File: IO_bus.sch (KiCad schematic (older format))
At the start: 2 parts

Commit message: Added missing signals to IO and added buffer
I've removed the /WAIT and also added a somewhat dodgy diode AND to
handle the bi-directional Dx buffer. Might work, might not.

Also cleaned up the buses and just tidied things up.
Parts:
- removed P?: CONN_01X16, symbol CONN_01X16
- added C?: 100n, symbol C
- added P?: CONN_01X14, symbol CONN_01X14
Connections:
- net labels added: VCC, ~CLK
- net labels removed: CLK, VCC_5V, ~WAIT
- wire segments 25 -> 28
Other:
- moved on the sheet: P?
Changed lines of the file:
@@
 $Descr A4 11693 8268
 encoding utf-8
-Sheet 9 16
+Sheet 11 16
 Title ""
 Date ""
@@
 Text HLabel 1850 2000 0    60   Input ~ 0
 ~WR
-Text HLabel 1850 2300 0    60   Input ~ 0
-CLK
+Text HLabel 1850 2200 0    60   Input ~ 0
+~CLK
 Text HLabel 1850 2100 0    60   BiDi ~ 0
 ~INT
-Text HLabel 1850 2200 0    60   BiDi ~ 0
-~WAIT
+Text HLabel 1800 3200 0    60   BiDi ~ 0
+D4
+Text HLabel 1800 3300 0    60   BiDi ~ 0
+D5
 Text HLabel 1800 3400 0    60   BiDi ~ 0
-D4
+D6
 Text HLabel 1800 3500 0    60   BiDi ~ 0
-D5
-Text HLabel 1800 3600 0    60   BiDi ~ 0
-D6
-Text HLabel 1800 3700 0    60   BiDi ~ 0
 D7
+Text HLabel 1800 2800 0    60   BiDi ~ 0
+D0
+Text HLabel 1800 2900 0    60   BiDi ~ 0
+D1
 Text HLabel 1800 3000 0    60   BiDi ~ 0
-D0
+D2
 Text HLabel 1800 3100 0    60   BiDi ~ 0
-D1
-Text HLabel 1800 3200 0    60   BiDi ~ 0
-D2
-Text HLabel 1800 3300 0    60   BiDi ~ 0
 D3
-Text HLabel 1850 2600 0    60   UnSpc ~ 0
-VCC_5V
-Text HLabel 1850 2700 0    60   UnSpc ~ 0
-GND
 Wire Wire Line
 	1850 1200 2100 1200
@@
 	1850 2100 2100 2100
 Wire Wire Line
-	2100 2200 1850 2200
-Wire Wire Line
-	1850 2300 2100 2300
-Wire Wire Line
-	1850 2700 2100 2700
-Wire Wire Line
-	1850 2600 2100 2600
-$Comp
-L CONN_01X16 P?
-U 1 1 57809941
-P 2300 1950
-F 0 "P?" H 2300 2800 50  0000 C CNN
-F 1 "CONN_01X16" V 2400 1950 50  0000 C CNN
-F 2 "" H 2300 1950 50  0000 C CNN
-F 3 "" H 2300 1950 50  0000 C CNN
-	1    2300 1950
-	1    0    0    -1
-$EndComp
+	1850 2200 2100 2200
+Wire Wire Line
+	1250 2500 2100 2500
 $Comp
 L CONN_01X08 P?
 U 1 1 57809978
-P 2300 3350
-F 0 "P?" H 2300 3800 50  0000 C CNN
-F 1 "CONN_01X08" V 2400 3350 50  0000 C CNN
-F 2 "" H 2300 3350 50  0000 C CNN
-F 3 "" H 2300 3350 50  0000 C CNN
-	1    2300 3350
-	1    0    0    -1
-$EndComp
+P 2300 3150
+AR Path="/578460AE/578087DE/57809978" Ref="P?"  Part="1"
+AR Path="/578460AE/57822535/57809978" Ref="P?"  Part="1"
+AR Path="/578460AE/57824229/57809978" Ref="P?"  Part="1"
+AR Path="/578460AE/57824279/57809978" Ref="P?"  Part="1"
+AR Path="/578460AE/578298A9/57809978" Ref="P?"  Part="1"
+AR Path="/578460AE/578298F9/57809978" Ref="P?"  Part="1"
+AR Path="/578460AE/57830D91/57809978" Ref="P?"  Part="1"
+AR Path="/578460AE/57831F66/57809978" Ref="P?"  Part="1"
+F 0 "P?" H 2300 3600 50  0000 C CNN
+F 1 "CONN_01X08" V 2400 3150 50  0000 C CNN
+F 2 "" H 2300 3150 50  0000 C CNN
+F 3 "" H 2300 3150 50  0000 C CNN
+	1    2300 3150
+	1    0    0    -1
+$EndComp
+Wire Wire Line
+	1800 2800 2100 2800
+Wire Wire Line
+	2100 2900 1800 2900
 Wire Wire Line
 	1800 3000 2100 3000
@@
 Wire Wire Line
 	2100 3500 1800 3500
-Wire Wire Line
-	1800 3600 2100 3600
-Wire Wire Line
-	2100 3700 1800 3700
-Text HLabel 1850 2500 0    60   Input ~ 0
+Text HLabel 1850 2300 0    60   Input ~ 0
 ~RESET
 Wire Wire Line
-	1850 2500 2100 2500
-Wire Wire Line
-	2050 2700 2050 2400
-Wire Wire Line
-	2050 2400 2100 2400
-Connection ~ 2050 2700
+	1850 2300 2100 2300
+Wire Wire Line
+	1000 2100 1000 2300
+Wire Wire Line
+	1000 2600 1000 2800
+$Comp
+L VCC #PWR?
+U 1 1 5783B273
+P 1000 2100
+AR Path="/578460AE/578087DE/5783B273" Ref="#PWR?"  Part="1"
+AR Path="/578460AE/57822535/5783B273" Ref="#PWR?"  Part="1"
+AR Path="/578460AE/57824229/5783B273" Ref="#PWR?"  Part="1"
+AR Path="/578460AE/57824279/5783B273" Ref="#PWR?"  Part="1"
+AR Path="/578460AE/578298A9/5783B273" Ref="#PWR?"  Part="1"
+AR Path="/578460AE/578298F9/5783B273" Ref="#PWR?"  Part="1"
+AR Path="/578460AE/57830D91/5783B273" Ref="#PWR?"  Part="1"
+AR Path="/578460AE/57831F66/5783B273" Ref="#PWR?"  Part="1"
+F 0 "#PWR?" H 1000 1950 50  0001 C CNN
+F 1 "VCC" H 1000 2250 50  0000 C CNN
+F 2 "" H 1000 2100 50  0000 C CNN
+F 3 "" H 1000 2100 50  0000 C CNN
+	1    1000 2100
+	1    0    0    -1
+$EndComp
+$Comp
+L GND #PWR?
+U 1 1 5783B28B
+P 1000 2800
+AR Path="/578460AE/578087DE/5783B28B" Ref="#PWR?"  Part="1"
+AR Path="/578460AE/57822535/5783B28B" Ref="#PWR?"  Part="1"
+AR Path="/578460AE/57824229/5783B28B" Ref="#PWR?"  Part="1"
+AR Path="/578460AE/57824279/5783B28B" Ref="#PWR?"  Part="1"
+AR Path="/578460AE/578298A9/5783B28B" Ref="#PWR?"  Part="1"
+AR Path="/578460AE/578298F9/5783B28B" Ref="#PWR?"  Part="1"
+AR Path="/578460AE/57830D91/5783B28B" Ref="#PWR?"  Part="1"
+AR Path="/578460AE/57831F66/5783B28B" Ref="#PWR?"  Part="1"
+F 0 "#PWR?" H 1000 2550 50  0001 C CNN
+F 1 "GND" H 1000 2650 50  0000 C CNN
+F 2 "" H 1000 2800 50  0000 C CNN
+F 3 "" H 1000 2800 50  0000 C CNN
+	1    1000 2800
+	1    0    0    -1
+$EndComp
+$Comp
+L C C?
+U 1 1 5783B2B3
+P 1000 2450
+AR Path="/578460AE/578087DE/5783B2B3" Ref="C?"  Part="1"
+AR Path="/578460AE/57822535/5783B2B3" Ref="C?"  Part="1"
+AR Path="/578460AE/57824229/5783B2B3" Ref="C?"  Part="1"
+AR Path="/578460AE/57824279/5783B2B3" Ref="C?"  Part="1"
+AR Path="/578460AE/578298A9/5783B2B3" Ref="C?"  Part="1"
+AR Path="/578460AE/578298F9/5783B2B3" Ref="C?"  Part="1"
+AR Path="/578460AE/57830D91/5783B2B3" Ref="C?"  Part="1"
+AR Path="/578460AE/57831F66/5783B2B3" Ref="C?"  Part="1"
+F 0 "C?" H 1025 2550 50  0000 L CNN
+F 1 "100n" H 1025 2350 50  0000 L CNN
+F 2 "" H 1038 2300 50  0000 C CNN
+F 3 "" H 1000 2450 50  0000 C CNN
+	1    1000 2450
+	1    0    0    -1
+$EndComp
+Wire Wire Line
+	2100 2400 1250 2400
+Wire Wire Line
+	1250 2400 1250 2200
+Wire Wire Line
+	1250 2200 1000 2200
+Connection ~ 1000 2200
+Wire Wire Line
+	1250 2500 1250 2700
+Wire Wire Line
+	1250 2700 1000 2700
+Connection ~ 1000 2700
+$Comp
+L CONN_01X14 P?
+U 1 1 5785DCD8
+P 2300 1850
+AR Path="/578460AE/578087DE/5785DCD8" Ref="P?"  Part="1"
+AR Path="/578460AE/57822535/5785DCD8" Ref="P?"  Part="1"
+AR Path="/578460AE/57824229/5785DCD8" Ref="P?"  Part="1"
+AR Path="/578460AE/57824279/5785DCD8" Ref="P?"  Part="1"
+AR Path="/578460AE/578298A9/5785DCD8" Ref="P?"  Part="1"
+AR Path="/578460AE/578298F9/5785DCD8" Ref="P?"  Part="1"
+AR Path="/578460AE/57830D91/5785DCD8" Ref="P?"  Part="1"
+AR Path="/578460AE/57831F66/5785DCD8" Ref="P?"  Part="1"
+F 0 "P?" H 2300 2600 50  0000 C CNN
+F 1 "CONN_01X14" V 2400 1850 50  0000 C CNN
+F 2 "" H 2300 1850 50  0000 C CNN
+F 3 "" H 2300 1850 50  0000 C CNN
+	1    2300 1850
+	1    0    0    -1
+$EndComp
 $EndSCHEMATC

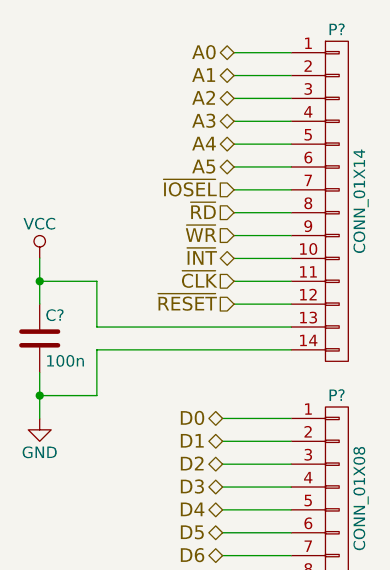
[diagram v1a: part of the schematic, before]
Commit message: Added /intack signal and a pri-encoder for /iosel
Brain fart on the diode crap. Was tired. Added a priority encoder to
enable the Dx buffer so it properly tristates when no IObus ports are
selected.

Added a NOR gate to provide a /intack signal for any board to properly
detect their interupt has been accepted but the z80. Boards will need to
figure out who the interupt is for.

Will have to add interupt priority pins to the boards to allow the
boards to put jump vectors onto the data bus to service the interrupt
This should be fairly easy, just means the service pritority of the
slots will be A-H, with A being the highest priority and H being the
lowest.

Going to replace the hex inverters with the spare NOR gates too.
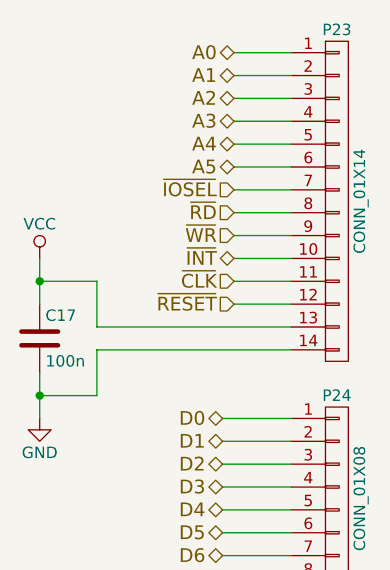
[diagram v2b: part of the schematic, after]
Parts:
- C10: renamed from C?; footprint (none) -> Capacitors_SMD:C_0805_HandSoldering
- P10: renamed from P?; footprint (none) -> Pin_Headers:Pin_Header_Straight_1x08
- P9: renamed from P?; footprint (none) -> Pin_Headers:Pin_Header_Straight_1x14
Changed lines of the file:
@@
 $Descr A4 11693 8268
 encoding utf-8
-Sheet 11 16
+Sheet 4 14
 Title ""
 Date ""
@@
 	1250 2500 2100 2500
 $Comp
-L CONN_01X08 P?
+L CONN_01X08 P10
 U 1 1 57809978
 P 2300 3150
-AR Path="/578460AE/578087DE/57809978" Ref="P?"  Part="1"
-AR Path="/578460AE/57822535/57809978" Ref="P?"  Part="1"
-AR Path="/578460AE/57824229/57809978" Ref="P?"  Part="1"
-AR Path="/578460AE/57824279/57809978" Ref="P?"  Part="1"
-AR Path="/578460AE/578298A9/57809978" Ref="P?"  Part="1"
-AR Path="/578460AE/578298F9/57809978" Ref="P?"  Part="1"
-AR Path="/578460AE/57830D91/57809978" Ref="P?"  Part="1"
-AR Path="/578460AE/57831F66/57809978" Ref="P?"  Part="1"
-F 0 "P?" H 2300 3600 50  0000 C CNN
+AR Path="/578460AE/578087DE/57809978" Ref="P10"  Part="1"
+AR Path="/578460AE/57822535/57809978" Ref="P12"  Part="1"
+AR Path="/578460AE/57824229/57809978" Ref="P14"  Part="1"
+AR Path="/578460AE/57824279/57809978" Ref="P16"  Part="1"
+AR Path="/578460AE/578298A9/57809978" Ref="P18"  Part="1"
+AR Path="/578460AE/578298F9/57809978" Ref="P20"  Part="1"
+AR Path="/578460AE/57830D91/57809978" Ref="P22"  Part="1"
+AR Path="/578460AE/57831F66/57809978" Ref="P24"  Part="1"
+F 0 "P24" H 2300 3600 50  0000 C CNN
 F 1 "CONN_01X08" V 2400 3150 50  0000 C CNN
-F 2 "" H 2300 3150 50  0000 C CNN
+F 2 "Pin_Headers:Pin_Header_Straight_1x08" H 2300 3150 50  0001 C CNN
 F 3 "" H 2300 3150 50  0000 C CNN
 	1    2300 3150
@@
 	1000 2600 1000 2800
 $Comp
-L VCC #PWR?
+L VCC #PWR027
 U 1 1 5783B273
 P 1000 2100
-AR Path="/578460AE/578087DE/5783B273" Ref="#PWR?"  Part="1"
-AR Path="/578460AE/57822535/5783B273" Ref="#PWR?"  Part="1"
-AR Path="/578460AE/57824229/5783B273" Ref="#PWR?"  Part="1"
-AR Path="/578460AE/57824279/5783B273" Ref="#PWR?"  Part="1"
-AR Path="/578460AE/578298A9/5783B273" Ref="#PWR?"  Part="1"
-AR Path="/578460AE/578298F9/5783B273" Ref="#PWR?"  Part="1"
-AR Path="/578460AE/57830D91/5783B273" Ref="#PWR?"  Part="1"
-AR Path="/578460AE/57831F66/5783B273" Ref="#PWR?"  Part="1"
-F 0 "#PWR?" H 1000 1950 50  0001 C CNN
+AR Path="/578460AE/578087DE/5783B273" Ref="#PWR027"  Part="1"
+AR Path="/578460AE/57822535/5783B273" Ref="#PWR029"  Part="1"
+AR Path="/578460AE/57824229/5783B273" Ref="#PWR031"  Part="1"
+AR Path="/578460AE/57824279/5783B273" Ref="#PWR033"  Part="1"
+AR Path="/578460AE/578298A9/5783B273" Ref="#PWR035"  Part="1"
+AR Path="/578460AE/578298F9/5783B273" Ref="#PWR037"  Part="1"
+AR Path="/578460AE/57830D91/5783B273" Ref="#PWR039"  Part="1"
+AR Path="/578460AE/57831F66/5783B273" Ref="#PWR041"  Part="1"
+F 0 "#PWR041" H 1000 1950 50  0001 C CNN
 F 1 "VCC" H 1000 2250 50  0000 C CNN
 F 2 "" H 1000 2100 50  0000 C CNN
@@
 $EndComp
 $Comp
-L GND #PWR?
+L GND #PWR028
 U 1 1 5783B28B
 P 1000 2800
-AR Path="/578460AE/578087DE/5783B28B" Ref="#PWR?"  Part="1"
-AR Path="/578460AE/57822535/5783B28B" Ref="#PWR?"  Part="1"
-AR Path="/578460AE/57824229/5783B28B" Ref="#PWR?"  Part="1"
-AR Path="/578460AE/57824279/5783B28B" Ref="#PWR?"  Part="1"
-AR Path="/578460AE/578298A9/5783B28B" Ref="#PWR?"  Part="1"
-AR Path="/578460AE/578298F9/5783B28B" Ref="#PWR?"  Part="1"
-AR Path="/578460AE/57830D91/5783B28B" Ref="#PWR?"  Part="1"
-AR Path="/578460AE/57831F66/5783B28B" Ref="#PWR?"  Part="1"
-F 0 "#PWR?" H 1000 2550 50  0001 C CNN
+AR Path="/578460AE/578087DE/5783B28B" Ref="#PWR028"  Part="1"
+AR Path="/578460AE/57822535/5783B28B" Ref="#PWR030"  Part="1"
+AR Path="/578460AE/57824229/5783B28B" Ref="#PWR032"  Part="1"
+AR Path="/578460AE/57824279/5783B28B" Ref="#PWR034"  Part="1"
+AR Path="/578460AE/578298A9/5783B28B" Ref="#PWR036"  Part="1"
+AR Path="/578460AE/578298F9/5783B28B" Ref="#PWR038"  Part="1"
+AR Path="/578460AE/57830D91/5783B28B" Ref="#PWR040"  Part="1"
+AR Path="/578460AE/57831F66/5783B28B" Ref="#PWR042"  Part="1"
+F 0 "#PWR042" H 1000 2550 50  0001 C CNN
 F 1 "GND" H 1000 2650 50  0000 C CNN
 F 2 "" H 1000 2800 50  0000 C CNN
@@
 $EndComp
 $Comp
-L C C?
+L C C10
 U 1 1 5783B2B3
 P 1000 2450
-AR Path="/578460AE/578087DE/5783B2B3" Ref="C?"  Part="1"
-AR Path="/578460AE/57822535/5783B2B3" Ref="C?"  Part="1"
-AR Path="/578460AE/57824229/5783B2B3" Ref="C?"  Part="1"
-AR Path="/578460AE/57824279/5783B2B3" Ref="C?"  Part="1"
-AR Path="/578460AE/578298A9/5783B2B3" Ref="C?"  Part="1"
-AR Path="/578460AE/578298F9/5783B2B3" Ref="C?"  Part="1"
-AR Path="/578460AE/57830D91/5783B2B3" Ref="C?"  Part="1"
-AR Path="/578460AE/57831F66/5783B2B3" Ref="C?"  Part="1"
-F 0 "C?" H 1025 2550 50  0000 L CNN
+AR Path="/578460AE/578087DE/5783B2B3" Ref="C10"  Part="1"
+AR Path="/578460AE/57822535/5783B2B3" Ref="C11"  Part="1"
+AR Path="/578460AE/57824229/5783B2B3" Ref="C12"  Part="1"
+AR Path="/578460AE/57824279/5783B2B3" Ref="C13"  Part="1"
+AR Path="/578460AE/578298A9/5783B2B3" Ref="C14"  Part="1"
+AR Path="/578460AE/578298F9/5783B2B3" Ref="C15"  Part="1"
+AR Path="/578460AE/57830D91/5783B2B3" Ref="C16"  Part="1"
+AR Path="/578460AE/57831F66/5783B2B3" Ref="C17"  Part="1"
+F 0 "C17" H 1025 2550 50  0000 L CNN
 F 1 "100n" H 1025 2350 50  0000 L CNN
-F 2 "" H 1038 2300 50  0000 C CNN
+F 2 "Capacitors_SMD:C_0805_HandSoldering" H 1038 2300 50  0001 C CNN
 F 3 "" H 1000 2450 50  0000 C CNN
 	1    1000 2450
@@
 Connection ~ 1000 2700
 $Comp
-L CONN_01X14 P?
+L CONN_01X14 P9
 U 1 1 5785DCD8
 P 2300 1850
-AR Path="/578460AE/578087DE/5785DCD8" Ref="P?"  Part="1"
-AR Path="/578460AE/57822535/5785DCD8" Ref="P?"  Part="1"
-AR Path="/578460AE/57824229/5785DCD8" Ref="P?"  Part="1"
-AR Path="/578460AE/57824279/5785DCD8" Ref="P?"  Part="1"
-AR Path="/578460AE/578298A9/5785DCD8" Ref="P?"  Part="1"
-AR Path="/578460AE/578298F9/5785DCD8" Ref="P?"  Part="1"
-AR Path="/578460AE/57830D91/5785DCD8" Ref="P?"  Part="1"
-AR Path="/578460AE/57831F66/5785DCD8" Ref="P?"  Part="1"
-F 0 "P?" H 2300 2600 50  0000 C CNN
+AR Path="/578460AE/578087DE/5785DCD8" Ref="P9"  Part="1"
+AR Path="/578460AE/57822535/5785DCD8" Ref="P11"  Part="1"
+AR Path="/578460AE/57824229/5785DCD8" Ref="P13"  Part="1"
+AR Path="/578460AE/57824279/5785DCD8" Ref="P15"  Part="1"
+AR Path="/578460AE/578298A9/5785DCD8" Ref="P17"  Part="1"
+AR Path="/578460AE/578298F9/5785DCD8" Ref="P19"  Part="1"
+AR Path="/578460AE/57830D91/5785DCD8" Ref="P21"  Part="1"
+AR Path="/578460AE/57831F66/5785DCD8" Ref="P23"  Part="1"
+F 0 "P23" H 2300 2600 50  0000 C CNN
 F 1 "CONN_01X14" V 2400 1850 50  0000 C CNN
-F 2 "" H 2300 1850 50  0000 C CNN
+F 2 "Pin_Headers:Pin_Header_Straight_1x14" H 2300 1850 50  0001 C CNN
 F 3 "" H 2300 1850 50  0000 C CNN
 	1    2300 1850

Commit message: Added interrupt priority pins to bus
These pins allow the boards to accept an interrupt assert priority of
the recieved interrupt ACK and load the data bus with a jump offset to
an ISR. Once a board has assert priority it sets it's IEO low so all
lower priority boards know the interrupt ACK wasn't for them and to try
again.

This will be a beast!
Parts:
- removed P9: CONN_01X14, Pin_Headers:Pin_Header_Straight_1x14, symbol CONN_01X14
- added P?: CONN_01X18, symbol CONN_01X18
- renumbered P10 to P12
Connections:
- net labels added: IEI, IEO, ~INTACK
- wire segments 28 -> 36
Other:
- note added: "Note: Interrupt Priority handling works as follows.\n\nIEI is the priority of this boards interrupt\n - if this is high the upsteam boards haven't claimed the interrupt and we can claim it (if required).\n - if this is low an upstream board has already claimed the interrupt.\n\nTo claim an interrupt pass a low to all lower priority boards by setting IEO low, otherwise set IEO to the state of IEI."
- moved on the sheet: C10, P?

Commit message: Removed the interrupt priority circuitry
After second thought the added complexity just wasn't worth it.
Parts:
- removed P?: CONN_01X18, symbol CONN_01X18
- added P9: CONN_01X14, symbol CONN_01X14
- renumbered P12 to P10
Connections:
- net labels removed: IEI, IEO, ~INTACK
- wire segments 36 -> 28
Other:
- note removed: "Note: Interrupt Priority handling works as follows.\n\nIEI is the priority of this boards interrupt\n - if this is high the upsteam boards haven't claimed the interrupt and we can claim it (if required).\n - if this is low an upstream board has already claimed the interrupt.\n\nTo claim an interrupt pass a low to all lower priority boards by setting IEO low, otherwise set IEO to the state of IEI."
- moved on the sheet: C17, P24

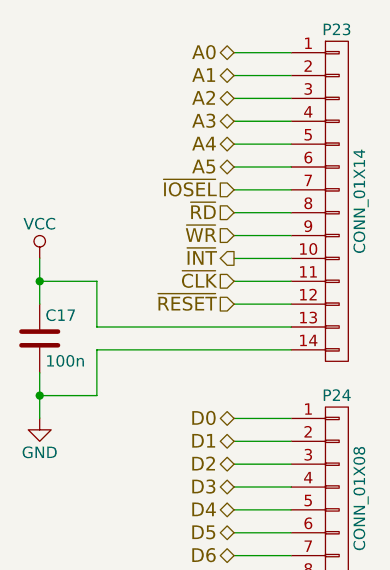
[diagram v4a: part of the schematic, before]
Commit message: Added basic board layout WIP
Switched a few bus lines around to make the layout a little easier.
Still learning PCBNew, has a few quirks I haven't figured out yet.
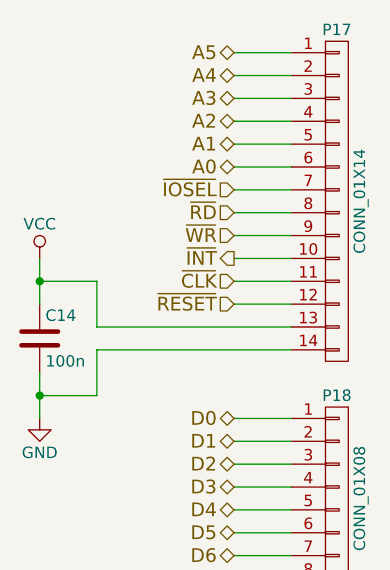
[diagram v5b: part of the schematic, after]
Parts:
- P9: footprint (none) -> Socket_Strips:Socket_Strip_Straight_1x14
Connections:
- net A0: now also P9.6 (P6); no longer P9.1 (P1)
- net A1: now also P9.5 (P5); no longer P9.2 (P2)
- net A2: now also P9.4 (P4); no longer P9.3 (P3)
- net A3: now also P9.3 (P3); no longer P9.4 (P4)
- net A4: now also P9.2 (P2); no longer P9.5 (P5)
- net A5: now also P9.1 (P1); no longer P9.6 (P6)
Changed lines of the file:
@@
 $Descr A4 11693 8268
 encoding utf-8
-Sheet 4 16
+Sheet 8 16
 Title ""
 Date ""
@@
 Comment4 ""
 $EndDescr
+Text HLabel 3250 2500 0    60   3State ~ 0
+A0
+Text HLabel 3250 2400 0    60   3State ~ 0
+A1
+Text HLabel 3250 2300 0    60   3State ~ 0
+A2
+Text HLabel 3250 2200 0    60   3State ~ 0
+A3
+Text HLabel 3250 2100 0    60   3State ~ 0
+A4
 Text HLabel 3250 2000 0    60   3State ~ 0
-A0
-Text HLabel 3250 2100 0    60   3State ~ 0
-A1
-Text HLabel 3250 2200 0    60   3State ~ 0
-A2
-Text HLabel 3250 2300 0    60   3State ~ 0
-A3
-Text HLabel 3250 2400 0    60   3State ~ 0
-A4
-Text HLabel 3250 2500 0    60   3State ~ 0
 A5
 Text HLabel 3250 2600 0    60   Input ~ 0
@@
 AR Path="/578460AE/57973E0B/57809978" Ref="P22"  Part="1"
 AR Path="/578460AE/57974892/57809978" Ref="P24"  Part="1"
-F 0 "P24" H 3700 4400 50  0000 C CNN
+F 0 "P18" H 3700 4400 50  0000 C CNN
 F 1 "CONN_01X08" V 3800 3950 50  0000 C CNN
 F 2 "Pin_Headers:Pin_Header_Straight_1x08" H 3700 3950 50  0001 C CNN
@@
 	2400 3400 2400 3600
 $Comp
-L VCC #PWR027
+L VCC #PWR030
 U 1 1 5783B273
 P 2400 2900
-AR Path="/578460AE/578087DE/5783B273" Ref="#PWR027"  Part="1"
+AR Path="/578460AE/578087DE/5783B273" Ref="#PWR030"  Part="1"
 AR Path="/578460AE/57822535/5783B273" Ref="#PWR029"  Part="1"
 AR Path="/578460AE/57824229/5783B273" Ref="#PWR031"  Part="1"
@@
 AR Path="/578460AE/57955FE5/5783B273" Ref="#PWR38"  Part="1"
 AR Path="/578460AE/57956D49/5783B273" Ref="#PWR40"  Part="1"
-AR Path="/578460AE/57970A38/5783B273" Ref="#PWR029"  Part="1"
-AR Path="/578460AE/57971583/5783B273" Ref="#PWR031"  Part="1"
-AR Path="/578460AE/579727D6/5783B273" Ref="#PWR033"  Part="1"
-AR Path="/578460AE/57972DE9/5783B273" Ref="#PWR035"  Part="1"
-AR Path="/578460AE/579734B0/5783B273" Ref="#PWR037"  Part="1"
-AR Path="/578460AE/57973E0B/5783B273" Ref="#PWR039"  Part="1"
-AR Path="/578460AE/57974892/5783B273" Ref="#PWR041"  Part="1"
-F 0 "#PWR041" H 2400 2750 50  0001 C CNN
+AR Path="/578460AE/57970A38/5783B273" Ref="#PWR032"  Part="1"
+AR Path="/578460AE/57971583/5783B273" Ref="#PWR034"  Part="1"
+AR Path="/578460AE/579727D6/5783B273" Ref="#PWR036"  Part="1"
+AR Path="/578460AE/57972DE9/5783B273" Ref="#PWR038"  Part="1"
+AR Path="/578460AE/579734B0/5783B273" Ref="#PWR040"  Part="1"
+AR Path="/578460AE/57973E0B/5783B273" Ref="#PWR042"  Part="1"
+AR Path="/578460AE/57974892/5783B273" Ref="#PWR044"  Part="1"
+F 0 "#PWR044" H 2400 2750 50  0001 C CNN
 F 1 "VCC" H 2400 3050 50  0000 C CNN
 F 2 "" H 2400 2900 50  0000 C CNN
@@
 $EndComp
 $Comp
-L GND #PWR028
+L GND #PWR031
 U 1 1 5783B28B
 P 2400 3600
-AR Path="/578460AE/578087DE/5783B28B" Ref="#PWR028"  Part="1"
+AR Path="/578460AE/578087DE/5783B28B" Ref="#PWR031"  Part="1"
 AR Path="/578460AE/57822535/5783B28B" Ref="#PWR030"  Part="1"
 AR Path="/578460AE/57824229/5783B28B" Ref="#PWR032"  Part="1"
@@
 AR Path="/578460AE/57955FE5/5783B28B" Ref="#PWR39"  Part="1"
 AR Path="/578460AE/57956D49/5783B28B" Ref="#PWR41"  Part="1"
-AR Path="/578460AE/57970A38/5783B28B" Ref="#PWR030"  Part="1"
-AR Path="/578460AE/57971583/5783B28B" Ref="#PWR032"  Part="1"
-AR Path="/578460AE/579727D6/5783B28B" Ref="#PWR034"  Part="1"
-AR Path="/578460AE/57972DE9/5783B28B" Ref="#PWR036"  Part="1"
-AR Path="/578460AE/579734B0/5783B28B" Ref="#PWR038"  Part="1"
-AR Path="/578460AE/57973E0B/5783B28B" Ref="#PWR040"  Part="1"
-AR Path="/578460AE/57974892/5783B28B" Ref="#PWR042"  Part="1"
-F 0 "#PWR042" H 2400 3350 50  0001 C CNN
+AR Path="/578460AE/57970A38/5783B28B" Ref="#PWR033"  Part="1"
+AR Path="/578460AE/57971583/5783B28B" Ref="#PWR035"  Part="1"
+AR Path="/578460AE/579727D6/5783B28B" Ref="#PWR037"  Part="1"
+AR Path="/578460AE/57972DE9/5783B28B" Ref="#PWR039"  Part="1"
+AR Path="/578460AE/579734B0/5783B28B" Ref="#PWR041"  Part="1"
+AR Path="/578460AE/57973E0B/5783B28B" Ref="#PWR043"  Part="1"
+AR Path="/578460AE/57974892/5783B28B" Ref="#PWR045"  Part="1"
+F 0 "#PWR045" H 2400 3350 50  0001 C CNN
 F 1 "GND" H 2400 3450 50  0000 C CNN
 F 2 "" H 2400 3600 50  0000 C CNN
@@
 AR Path="/578460AE/57973E0B/5783B2B3" Ref="C16"  Part="1"
 AR Path="/578460AE/57974892/5783B2B3" Ref="C17"  Part="1"
-F 0 "C17" H 2425 3350 50  0000 L CNN
+F 0 "C14" H 2425 3350 50  0000 L CNN
 F 1 "100n" H 2425 3150 50  0000 L CNN
 F 2 "Capacitors_SMD:C_0805_HandSoldering" H 2438 3100 50  0001 C CNN
@@
 AR Path="/578460AE/57973E0B/5796F695" Ref="P21"  Part="1"
 AR Path="/578460AE/57974892/5796F695" Ref="P23"  Part="1"
-F 0 "P23" H 3700 3400 50  0000 C CNN
+F 0 "P17" H 3700 3400 50  0000 C CNN
 F 1 "CONN_01X14" V 3800 2650 50  0000 C CNN
-F 2 "" H 3700 2650 50  0000 C CNN
+F 2 "Socket_Strips:Socket_Strip_Straight_1x14" H 3700 2650 50  0001 C CNN
 F 3 "" H 3700 2650 50  0000 C CNN
 	1    3700 2650
